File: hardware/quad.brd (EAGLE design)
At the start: 62 parts, among them IC1 BNO055, J501 I2C_TEST, U101 STM32F427VGT6, U201 LD1117, U202 AND_GATE, U203 SN74AHC1G32DBVR, U401 FT232R, U402 USB-MICROB", U403 LD1117, X101 24MHz, Y501 32.768kHz

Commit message: First draft schematic done
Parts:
- added R701: 10k, quad:R0603
- added U$2: PSMN9RS-30YLC, quad:SOT669
- added U404: MFS201N-16-Z, quad:MFS201N-16-Z
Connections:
- removed net N$3: U$1.PWR
- new net KILL_GND: ESC1.GND, ESC2.GND, ESC3.GND, ESC4.GND, U$2.MB
- new net POWER_EN: R701.2, U$2.4, U404.5
- net GND: now also R701.1, U$2.1, U$2.2, U$2.3; no longer ESC1.GND, ESC2.GND, ESC3.GND, ESC4.GND
- net VBATT: now also U$1.PWR, U404.3
- net VBUS: now also U404.1, U404.2
- net XBEE_DIO4: now also U404.6
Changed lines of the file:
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@@
 <element name="J501" library="quad" package="1X02" value="I2C_TEST" x="-267.462" y="-370.586"/>
 <element name="U$1" library="quad" package="XT60" value="XT60" x="-306.578" y="-344.424"/>
+<element name="U404" library="quad" package="MFS201N-16-Z" value="MFS201N-16-Z" x="-314.96" y="-391.922"/>
+<element name="U$2" library="quad" package="SOT669" value="PSMN9RS-30YLC" x="-328.676" y="-410.21"/>
+<element name="R701" library="quad" package="R0603" value="10k" x="-335.026" y="-417.322"/>
 </elements>
 <signals>
@@
 <via x="50.038" y="15.24" extent="1-16" drill="0.35"/>
 <contactref element="ESC3" pad="PWM_GND"/>
-<contactref element="ESC3" pad="GND"/>
-<contactref element="ESC1" pad="GND"/>
-<contactref element="ESC2" pad="GND"/>
-<contactref element="ESC4" pad="GND"/>
 <contactref element="ESC4" pad="PWM_GND"/>
 <contactref element="ESC2" pad="PWM_GND"/>
@@
 <contactref element="R503" pad="2"/>
 <contactref element="U$1" pad="GND"/>
+<contactref element="U$2" pad="2"/>
+<contactref element="U$2" pad="1"/>
+<contactref element="U$2" pad="3"/>
+<contactref element="R701" pad="1"/>
 <wire x1="-249.21" y1="-255.56" x2="-251.71" y2="-255.56" width="0" layer="19" extent="1-1"/>
 <wire x1="-249.21" y1="-254.75" x2="-249.21" y2="-255.56" width="0" layer="19" extent="1-1"/>
@@
 <wire x1="-273.978" y1="-339.852" x2="-273.978" y2="-334.772" width="0" layer="19" extent="1-1"/>
 <wire x1="-306.578" y1="-348.174" x2="-273.978" y2="-339.852" width="0" layer="19" extent="1-1"/>
-<wire x1="-208.026" y1="91.186" x2="-223.68" y2="-167.946" width="0" layer="19" extent="1-1"/>
-<wire x1="-195.326" y1="95.631" x2="-208.026" y2="91.186" width="0" layer="19" extent="1-1"/>
-<wire x1="-142.494" y1="91.186" x2="-195.326" y2="95.631" width="0" layer="19" extent="1-1"/>
-<wire x1="-129.794" y1="95.631" x2="-142.494" y2="91.186" width="0" layer="19" extent="1-1"/>
-<wire x1="-76.962" y1="91.186" x2="-129.794" y2="95.631" width="0" layer="19" extent="1-1"/>
-<wire x1="-64.262" y1="95.631" x2="-76.962" y2="91.186" width="0" layer="19" extent="1-1"/>
-<wire x1="-11.43" y1="91.186" x2="-64.262" y2="95.631" width="0" layer="19" extent="1-1"/>
-<wire x1="1.27" y1="95.631" x2="-11.43" y2="91.186" width="0" layer="19" extent="1-1"/>
+<wire x1="-328.041" y1="-412.935" x2="-306.578" y2="-348.174" width="0" layer="19" extent="1-1"/>
+<wire x1="-329.311" y1="-412.935" x2="-328.041" y2="-412.935" width="0" layer="19" extent="1-1"/>
+<wire x1="-330.581" y1="-412.935" x2="-329.311" y2="-412.935" width="0" layer="19" extent="1-1"/>
+<wire x1="-335.876" y1="-417.322" x2="-330.581" y2="-412.935" width="0" layer="19" extent="1-1"/>
+<wire x1="-195.326" y1="95.631" x2="-223.68" y2="-167.946" width="0" layer="19" extent="1-1"/>
+<wire x1="-129.794" y1="95.631" x2="-195.326" y2="95.631" width="0" layer="19" extent="1-1"/>
+<wire x1="-64.262" y1="95.631" x2="-129.794" y2="95.631" width="0" layer="19" extent="1-1"/>
+<wire x1="1.27" y1="95.631" x2="-64.262" y2="95.631" width="0" layer="19" extent="1-1"/>
 <wire x1="34.036" y1="31.408" x2="1.27" y2="95.631" width="0" layer="19" extent="1-1"/>
 <wire x1="52.23095625" y1="32.605040625" x2="34.036" y2="31.408" width="0" layer="19" extent="1-1"/>
@@
 <contactref element="C213" pad="1"/>
 <contactref element="U201" pad="3"/>
+<contactref element="U404" pad="3"/>
+<contactref element="U$1" pad="PWR"/>
+<wire x1="-306.578" y1="-340.674" x2="-310.96" y2="-393.172" width="0" layer="19" extent="1-1"/>
+<wire x1="-228.688" y1="-173.736" x2="-306.578" y2="-340.674" width="0" layer="19" extent="1-1"/>
 <wire x1="-218.28" y1="-167.946" x2="-228.688" y2="-173.736" width="0" layer="19" extent="1-1"/>
 <wire x1="-187.706" y1="91.186" x2="-218.28" y2="-167.946" width="0" layer="19" extent="1-1"/>
@@
 <contactref element="C405" pad="1"/>
 <contactref element="U403" pad="3"/>
+<contactref element="U404" pad="2"/>
+<contactref element="U404" pad="1"/>
 <wire x1="-234.282" y1="-245.162" x2="-244.69" y2="-250.952" width="0" layer="19" extent="1-1"/>
 <wire x1="-244.69" y1="-232.664" x2="-234.282" y2="-245.162" width="0" layer="19" extent="1-1"/>
@@
 <wire x1="-238.164" y1="-203.708" x2="-242.99" y2="-222.504" width="0" layer="19" extent="1-1"/>
 <wire x1="-222.037" y1="-186.875" x2="-238.164" y2="-203.708" width="0" layer="19" extent="1-1"/>
+<wire x1="-314.96" y1="-393.172" x2="-244.69" y2="-250.952" width="0" layer="19" extent="1-1"/>
+<wire x1="-318.96" y1="-393.172" x2="-314.96" y2="-393.172" width="0" layer="19" extent="1-1"/>
 </signal>
 <signal name="USBDM">
@@
 <signal name="VDDIO">
 </signal>
-<signal name="N$3">
-<contactref element="U$1" pad="PWR"/>
-</signal>
 <signal name="XBEE_DIO4">
 <contactref element="XB1" pad="11"/>
+<contactref element="U404" pad="6"/>
+<wire x1="-310.96" y1="-390.672" x2="-225.982" y2="-283.32" width="0" layer="19" extent="1-1"/>
 </signal>
 <signal name="XBEE_DIO0">
@@
 <contactref element="U101" pad="55"/>
 </signal>
+<signal name="POWER_EN">
+<contactref element="U404" pad="5"/>
+<contactref element="U$2" pad="4"/>
+<contactref element="R701" pad="2"/>
+<wire x1="-326.771" y1="-412.935" x2="-334.176" y2="-417.322" width="0" layer="19" extent="1-1"/>
+<wire x1="-314.96" y1="-390.672" x2="-326.771" y2="-412.935" width="0" layer="19" extent="1-1"/>
+</signal>
+<signal name="KILL_GND">
+<contactref element="U$2" pad="MB"/>
+<contactref element="ESC1" pad="GND"/>
+<contactref element="ESC3" pad="GND"/>
+<contactref element="ESC4" pad="GND"/>
+<contactref element="ESC2" pad="GND"/>
+<wire x1="-208.026" y1="91.186" x2="-328.676" y2="-409.01" width="0" layer="19" extent="1-1"/>
+<wire x1="-142.494" y1="91.186" x2="-208.026" y2="91.186" width="0" layer="19" extent="1-1"/>
+<wire x1="-76.962" y1="91.186" x2="-142.494" y2="91.186" width="0" layer="19" extent="1-1"/>
+<wire x1="-11.43" y1="91.186" x2="-76.962" y2="91.186" width="0" layer="19" extent="1-1"/>
+</signal>
 </signals>

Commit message: Fixes and start layout
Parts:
- removed C212, C213: 10uF, quad:C0603
- removed U201: LD1117, quad:SOT223
- added ASSOC, PWR: LED, quad:LED-0603
- added R4: 270, quad:R0603
- added R5: (no value), quad:R0603
- C205, C206, C207, C208, C209, C210, C401, C402, C403: value 100nF -> 0.1uF
- C211: value 100nF -> 4.7uF
- U402: value USB-MICROB" -> USB-MICROB; device quad:USB-B-MICRO-SMD_V03 -> quad:USB-B-MICRO-SMD
- moved R701 563.7 mm to (-31.0, 57.4)
- moved U404 540.8 mm to (-31.0, 68.3), turned to 225 degrees
- moved U$2 507.3 mm to (-57.9, 18.8)
- moved U$1 470.5 mm to (-50.0, 50.0), turned to 315 degrees
- moved MOT4 397.2 mm to (185.2, -1.02), turned to 270 degrees
- moved U402 388.8 mm to (61.5, 61.7), turned to 135 degrees
- moved U401 365.8 mm to (50.5, 52.3), turned to 225 degrees
- moved IC1 357.4 mm to (0.00, 0.00)
- moved MOT1 339.9 mm to (3.81, 170.7)
- moved MOT3 250.4 mm to (0.25, -150.6), turned to 180 degrees
- moved ESC4 241.7 mm to (101.6, 0.00), turned to 90 degrees
- moved ESC3 175.5 mm to (0.00, -101.6)
- moved MOT2 143.5 mm to (-165.6, 1.02), turned to 90 degrees
- moved ESC2 113.8 mm to (-101.6, 0.00), turned to 270 degrees
- moved U101 42.6 mm to (35.3, -2.16)
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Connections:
- new net N$17: R4.2, XB1.15
- new net N$18: PWR.C, R5.2
- new net N$3: ASSOC.A, R4.1
- net GND: now also ASSOC.C, R5.1, U402.SHIELD1, U402.SHIELD2; no longer C212.2, C213.2, U201.1
- net VBATT: no longer C213.1, U201.3
- net VDD_3V3: now also PWR.A; no longer C212.1, U201.2, U201.4
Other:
- board outline added: 407.9 x 384.6 mm

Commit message: Add board outline and make some placements
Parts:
- removed BNO055_NBOOT_LOAD, BNO055_NRESET: TESTPAD, quad:TESTPAD
- removed R1, R2, R3: 10k, quad:R0603
- removed R4: 270, quad:R0603
- added BNO_NBOOTLD, BNO_NRST: TESTPAD, quad:TESTPAD
- added EN: LED, quad:LED-0603
- added R504, R505, R506: 10k, quad:R0603
- added R601, R702: 270, quad:R0603
- R5: value (none) -> 270
- moved R5 496.3 mm to (-20.1, 31.1)
- moved PWR 494.1 mm to (-15.7, 31.0)
- moved J501 461.0 mm to (6.99, -0.13), turned to 270 degrees
- moved R501 432.0 mm to (-24.4, 25.1)
- moved R502 432.0 mm to (-24.4, 17.3)
- moved R503 432.0 mm to (-24.4, 12.2)
- moved C503 429.0 mm to (4.19, 5.08), turned to 270 degrees
- moved C504 420.0 mm to (-5.46, 5.08), turned to 270 degrees
- moved Y501 416.2 mm to (-0.76, 6.99), turned to 90 degrees
- moved C406 409.9 mm to (57.1, 22.2), turned to 45 degrees
- moved C502 406.2 mm to (-8.26, 3.05)
- moved C501 404.2 mm to (-17.5, 13.0)
- moved C405 394.0 mm to (43.9, 18.2), turned to 225 degrees
- moved C404 392.7 mm to (46.9, 31.4), turned to 45 degrees
- moved U203 389.8 mm to (-5.08, -9.53), turned to 315 degrees
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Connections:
- net USBDM renamed USB_D_N
- net USBDP renamed USB_D_P
- new net N$19: EN.C, R702.2
- new net PWR: C405.1, U403.3, U404.2
- net GND: now also U402.SHIELD3, U402.SHIELD4, U402.SHIELD5, U402.SHIELD6
- net I2C1_SCL: now also R506.2; no longer R3.2
- net I2C1_SDA: now also R505.2; no longer R2.2
- net KILL_GND: now also R702.1
- net N$13: now also BNO_NRST.P$1; no longer BNO055_NRESET.P$1
- net N$16: now also BNO_NBOOTLD.P$1, R504.1; no longer BNO055_NBOOT_LOAD.P$1, R1.1
- net N$17: now also R601.2; no longer R4.2
- net N$3: now also R601.1; no longer R4.1
- net PB12: no longer IC1.14
- net PD2: now also IC1.14
- net VBUS: now also U402.VBUS; no longer C405.1, U403.3, U404.2
- net VDD_3V3: now also EN.A, R504.2, R505.1, R506.1; no longer R1.2, R2.1, R3.1
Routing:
- net VBATT: track 0.00 -> 251.2 mm
- net KILL_GND: track 0.00 -> 163.9 mm, vias 0 -> 1
- net VBUS: track 0.00 -> 32.3 mm
- net I2C1_SDA: track 0.00 -> 19.7 mm, vias 0 -> 2
- net VDD_3V3: track 99.9 -> 118.8 mm
- net I2C1_SCL: track 0.00 -> 18.4 mm
- net USB_D_P: track 0.00 -> 16.6 mm
- net USB_D_N: track 0.00 -> 15.4 mm
- net MOT_4_3: track 0.00 -> 15.0 mm
- net MOT_4_1: track 0.00 -> 15.0 mm
- net MOT_3_3: track 0.00 -> 15.0 mm
- net MOT_3_1: track 0.00 -> 15.0 mm
- net MOT_2_3: track 0.00 -> 15.0 mm
- net MOT2_1: track 0.00 -> 15.0 mm
- net MOT1_3: track 0.00 -> 15.0 mm
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- added copper zone on layer 1, net GND
- removed copper zone on layer 1, net VDD_3V3
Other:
- board size 407.9 x 384.6 mm -> 254 x 254 mm

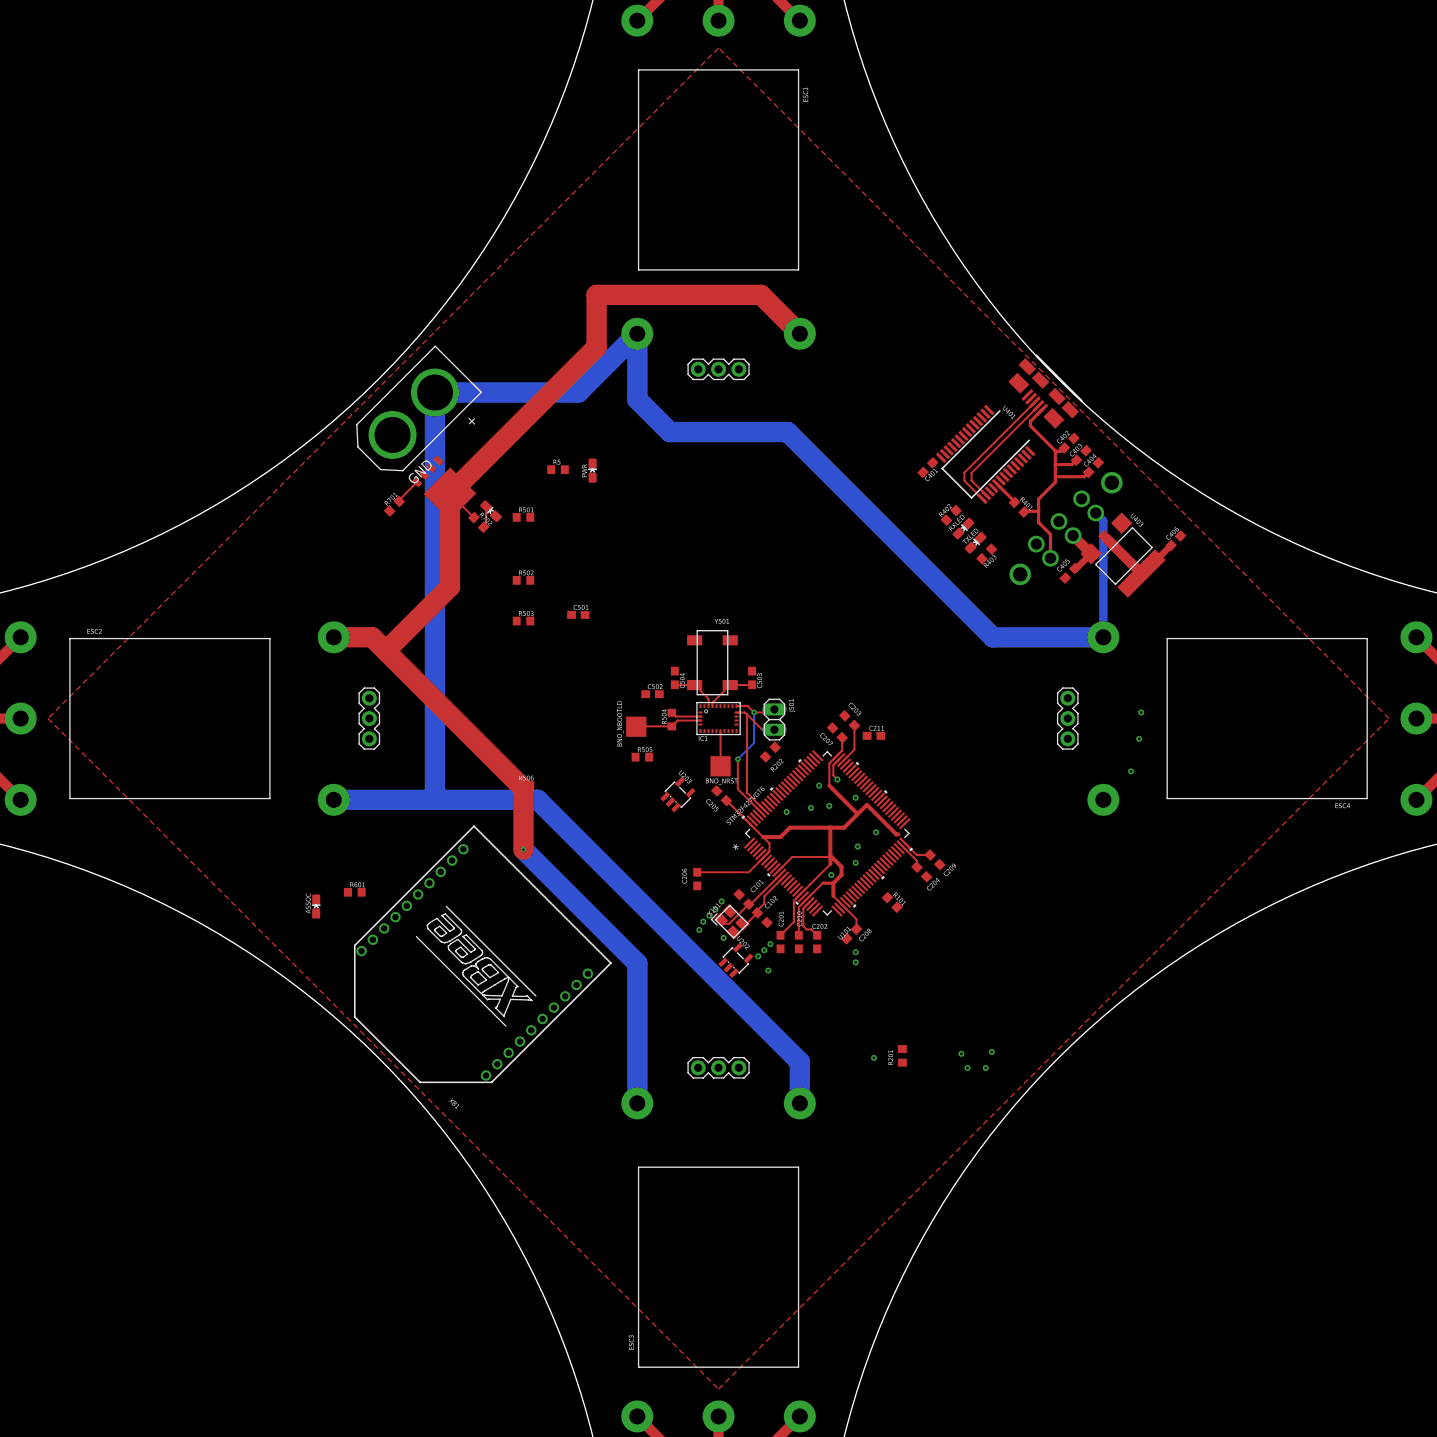
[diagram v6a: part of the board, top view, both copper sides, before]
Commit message: Passing DRC on the layout
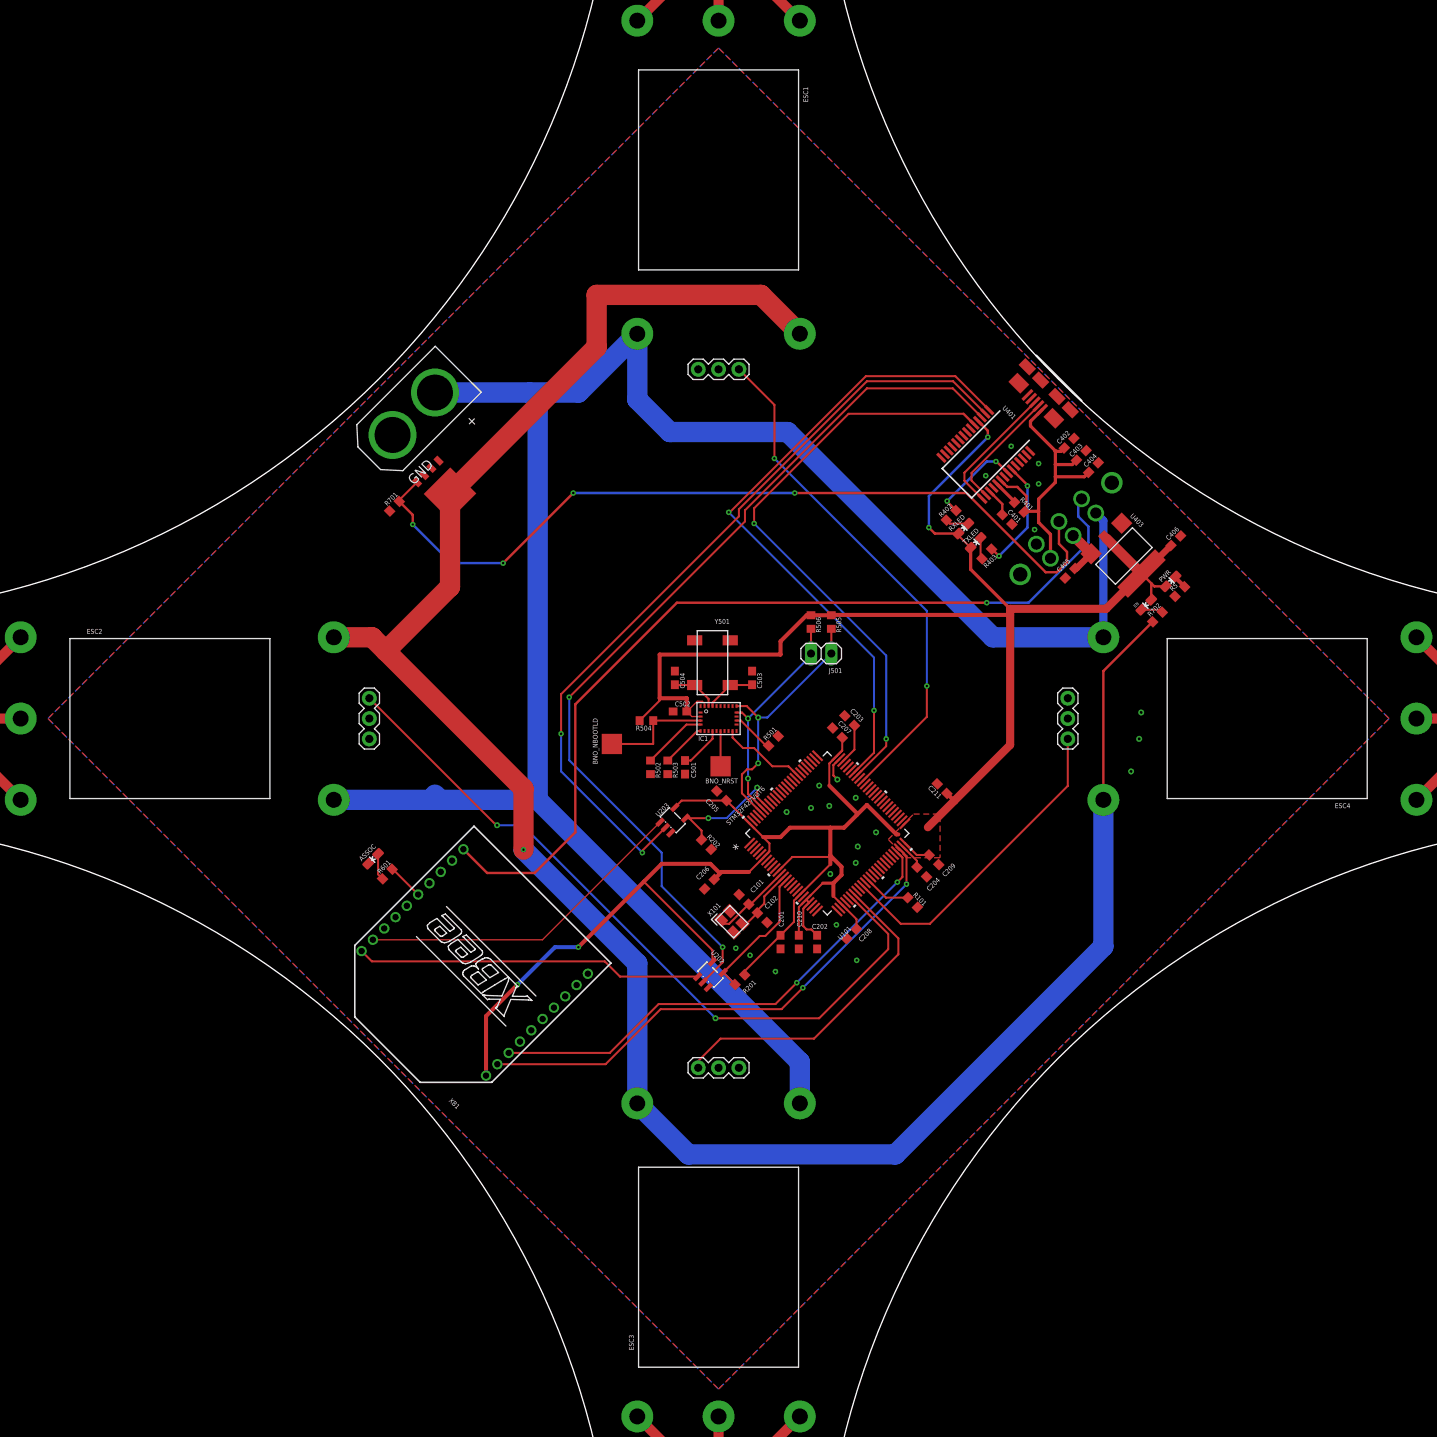
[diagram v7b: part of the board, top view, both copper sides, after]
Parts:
- moved R702 85.7 mm to (54.9, 12.7), turned to 45 degrees
- moved EN 82.7 mm to (53.5, 14.2), turned to 135 degrees
- moved R5 79.2 mm to (57.7, 15.9), turned to 45 degrees
- moved PWR 73.6 mm to (56.5, 17.1), turned to 315 degrees
- moved R501 41.9 mm to (6.86, -2.79), turned to 45 degrees
- moved R506 41.4 mm to (11.6, 12.1), turned to 270 degrees
- moved R505 29.0 mm to (14.1, 12.1), turned to 270 degrees
- moved R502 28.3 mm to (-8.51, -6.10), turned to 270 degrees
- moved R503 25.7 mm to (-6.35, -6.10), turned to 270 degrees
- moved C501 23.3 mm to (-4.19, -6.10), turned to 90 degrees
- moved R201 22.4 mm to (2.67, -32.6), turned to 45 degrees
- moved R202 14.1 mm to (-1.52, -15.7), turned to 315 degrees
- moved C401 11.8 mm to (36.1, 24.9), turned to 315 degrees
- moved C211 10.8 mm to (27.9, -8.76), turned to 135 degrees
- moved J501 10.1 mm to (12.8, 8.13), turned to 180 degrees
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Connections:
- removed net I2C2_SCL: U101.47
- removed net I2C2_SDA: U101.48
- removed net I2C3_SDA: U101.66
- removed net PB0: U101.35
- removed net PWM1: ESC1.PWM
- removed net PWM2: ESC2.PWM
- removed net PWM3: ESC3.PWM
- removed net PWM4: ESC4.PWM
- removed net SPI1_MISO: U101.31
- removed net SPI1_MOSI: U101.32
- new net PC10: U101.78
- new net PC11: U101.79
- new net TIM3_CH1: ESC2.PWM, U101.31
- new net TIM3_CH2: ESC3.PWM, U101.32
- new net TIM3_CH3: ESC4.PWM, U101.35
- new net TIM3_CH4: ESC1.PWM, U101.66
- net USART3_RX: now also U101.48; no longer U101.79
- net USART3_TX: now also U101.47; no longer U101.78
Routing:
- net VDD_3V3: track 118.8 -> 342.2 mm, vias 0 -> 4
- net FT232_RTS: track 0.00 -> 114.4 mm, vias 0 -> 2
- net XBEE_DIO4: track 0.00 -> 112.0 mm, vias 0 -> 1
- net KILL_GND: track 163.9 -> 274.4 mm
- net POWER_EN: track 3.31 -> 104.4 mm, vias 0 -> 4
- net FT232_DTR: track 0.00 -> 99.8 mm, vias 0 -> 2
- net TIM3_CH1: track 0.00 -> 93.5 mm, vias 0 -> 2
- net USART1_RX: track 0.00 -> 82.5 mm, vias 0 -> 2
- net USART1_TX: track 0.00 -> 74.8 mm, vias 0 -> 2
- net USART3_RX: track 0.00 -> 65.3 mm, vias 0 -> 2
- net TIM3_CH4: track 0.00 -> 64.6 mm, vias 0 -> 2
- net USART3_TX: track 0.00 -> 61.8 mm, vias 0 -> 2
- net XBEE_DIO0: track 0.00 -> 43.3 mm
- net XBEE_DIO1: track 0.00 -> 42.0 mm
- net TIM3_CH2: track 0.00 -> 41.2 mm
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- added copper zone on layer 16, net GND
- added copper zone on layer 1, net VDD_3V3
